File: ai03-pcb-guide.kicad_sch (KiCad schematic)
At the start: 24 parts, among them SW1 SW_Push, U1 ATmega32U4-A, Y1 16MHz

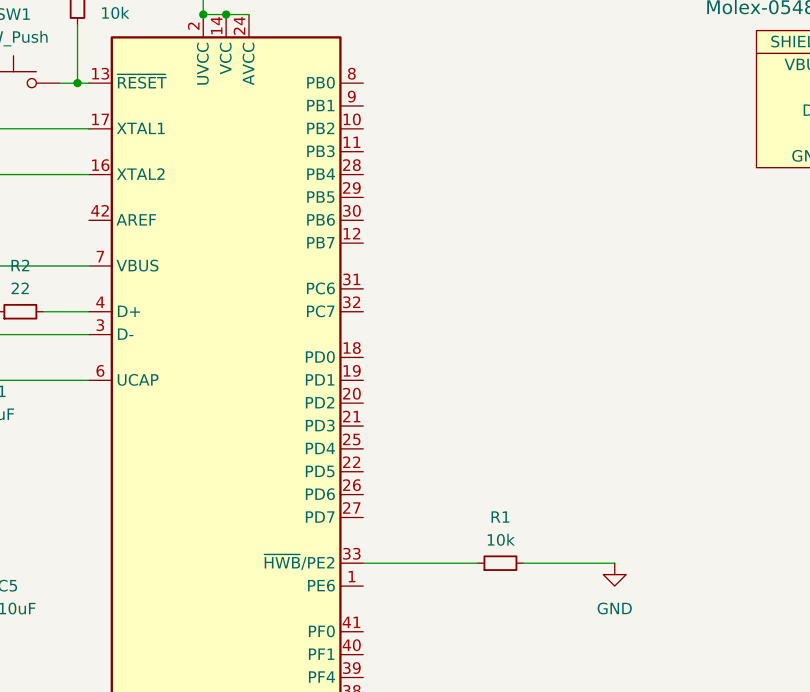
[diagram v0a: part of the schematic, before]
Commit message: added matrix to mcu pins
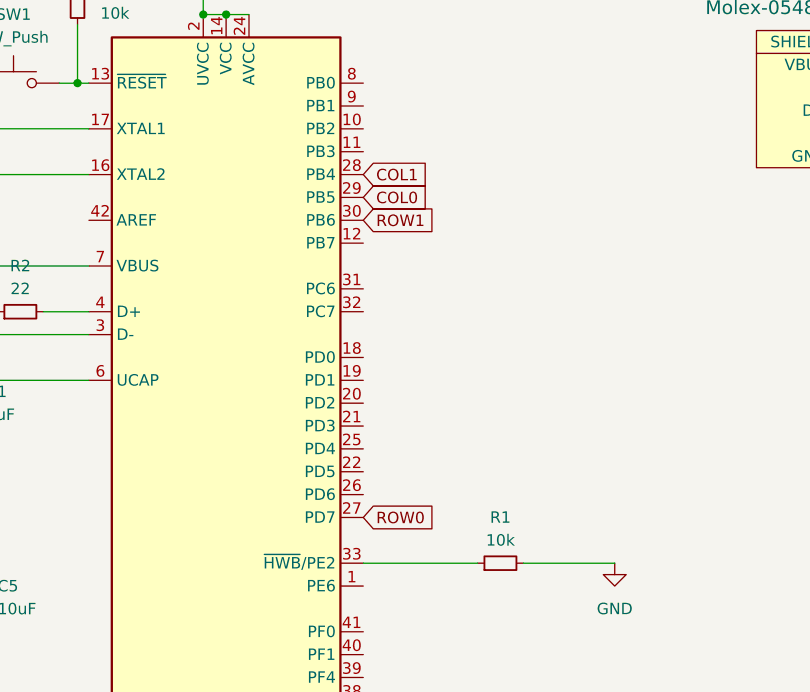
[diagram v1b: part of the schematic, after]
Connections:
- net COL0: now also U1.29 (PB5)
- net COL1: now also U1.28 (PB4)
- net ROW0: now also U1.27 (PD7)
- net ROW1: now also U1.30 (PB6)
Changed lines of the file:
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@@
+    )
+  )
+  (global_label "ROW0" (shape input) (at 120.142 90.932 0) (fields_autoplaced)
+    (effects (font (size 1.27 1.27)) (justify left))
+    (property "Intersheetrefs" "${INTERSHEET_REFS}" (at 128.3886 90.932 0)
+      (effects (font (size 1.27 1.27)) (justify left) hide)
     )
   )
@@
     (property "Intersheetrefs" "${INTERSHEET_REFS}" (at 56.1968 70.612 0)
       (effects (font (size 1.27 1.27)) (justify right) hide)
+    )
+  )
+  (global_label "ROW1" (shape input) (at 120.142 57.912 0) (fields_autoplaced)
+    (effects (font (size 1.27 1.27)) (justify left))
+    (property "Intersheetrefs" "${INTERSHEET_REFS}" (at 128.3886 57.912 0)
+      (effects (font (size 1.27 1.27)) (justify left) hide)
+    )
+  )
+  (global_label "COL1" (shape input) (at 120.142 52.832 0) (fields_autoplaced)
+    (effects (font (size 1.27 1.27)) (justify left))
+    (property "Intersheetrefs" "${INTERSHEET_REFS}" (at 127.9653 52.832 0)
+      (effects (font (size 1.27 1.27)) (justify left) hide)
     )
   )
@@
     )
   )
+  (global_label "COL0" (shape input) (at 120.142 55.372 0) (fields_autoplaced)
+    (effects (font (size 1.27 1.27)) (justify left))
+    (property "Intersheetrefs" "${INTERSHEET_REFS}" (at 127.9653 55.372 0)
+      (effects (font (size 1.27 1.27)) (justify left) hide)
+    )
+  )
